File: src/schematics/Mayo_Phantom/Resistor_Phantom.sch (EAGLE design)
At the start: 178 parts, among them J1 22-27-2041-04, K1 AQY22SOP, K2 AQY22SOP, K3 AQY22SOP, X1 DSUBIN

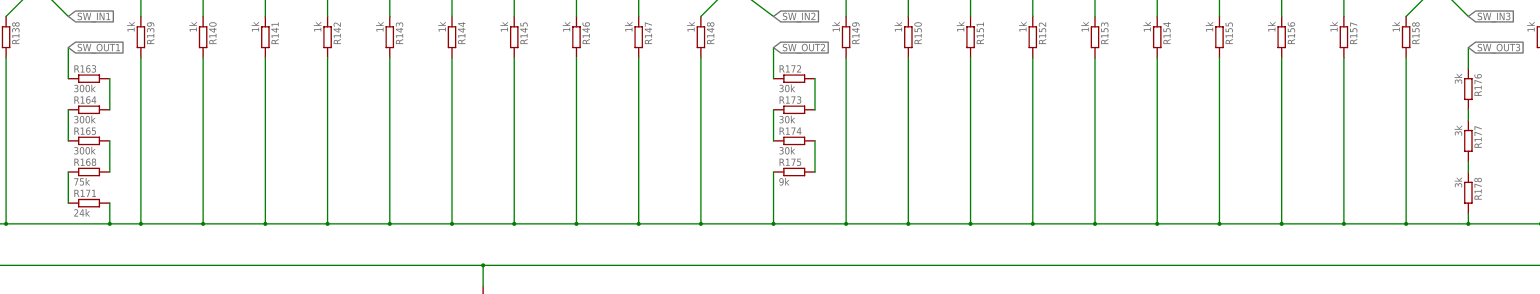
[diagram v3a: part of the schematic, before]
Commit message: changed resistor values in schematic
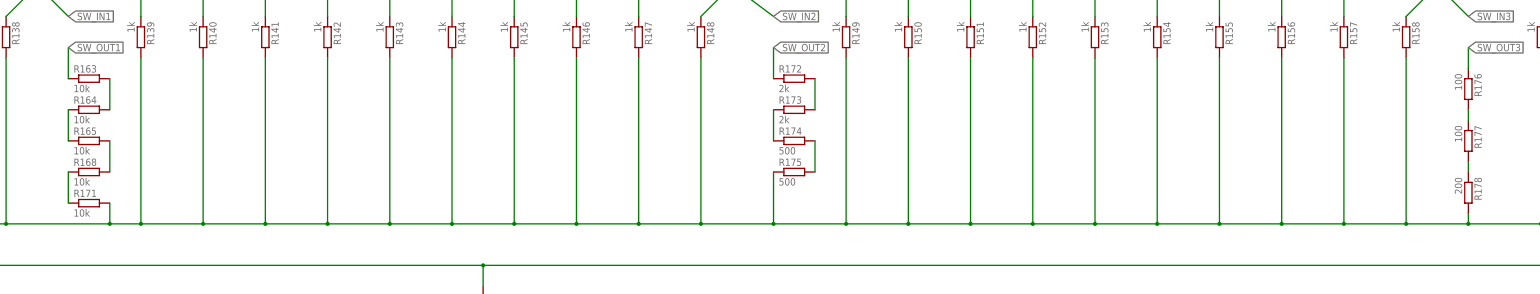
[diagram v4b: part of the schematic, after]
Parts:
- R163, R164, R165: value 300k -> 10k
- R168: value 75k -> 10k
- R171: value 24k -> 10k
- R172, R173: value 30k -> 2k
- R174: value 30k -> 500
- R175: value 9k -> 500
- R176, R177: value 3k -> 100
- R178: value 3k -> 200
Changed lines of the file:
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@@
 <grid distance="0.1" unitdist="inch" unit="inch" style="lines" multiple="1" display="no" altdistance="0.01" altunitdist="inch" altunit="inch"/>
 <layers>
-<layer number="1" name="Top" color="4" fill="1" visible="yes" active="no"/>
-<layer number="2" name="Route2" color="1" fill="3" visible="yes" active="no"/>
-<layer number="3" name="Route3" color="4" fill="3" visible="yes" active="no"/>
-<layer number="4" name="Route4" color="1" fill="4" visible="yes" active="no"/>
-<layer number="5" name="Route5" color="4" fill="4" visible="yes" active="no"/>
-<layer number="6" name="Route6" color="1" fill="8" visible="yes" active="no"/>
-<layer number="7" name="Route7" color="4" fill="8" visible="yes" active="no"/>
-<layer number="8" name="Route8" color="1" fill="2" visible="yes" active="no"/>
-<layer number="9" name="Route9" color="4" fill="2" visible="yes" active="no"/>
-<layer number="10" name="Route10" color="1" fill="7" visible="yes" active="no"/>
-<layer number="11" name="Route11" color="4" fill="7" visible="yes" active="no"/>
-<layer number="12" name="Route12" color="1" fill="5" visible="yes" active="no"/>
-<layer number="13" name="Route13" color="4" fill="5" visible="yes" active="no"/>
-<layer number="14" name="Route14" color="1" fill="6" visible="yes" active="no"/>
-<layer number="15" name="Route15" color="4" fill="6" visible="yes" active="no"/>
-<layer number="16" name="Bottom" color="1" fill="1" visible="yes" active="no"/>
-<layer number="17" name="Pads" color="2" fill="1" visible="yes" active="no"/>
-<layer number="18" name="Vias" color="2" fill="1" visible="yes" active="no"/>
-<layer number="19" name="Unrouted" color="6" fill="1" visible="yes" active="no"/>
-<layer number="20" name="Dimension" color="15" fill="1" visible="yes" active="no"/>
-<layer number="21" name="tPlace" color="7" fill="1" visible="yes" active="no"/>
-<layer number="22" name="bPlace" color="7" fill="1" visible="yes" active="no"/>
-<layer number="23" name="tOrigins" color="15" fill="1" visible="yes" active="no"/>
-<layer number="24" name="bOrigins" color="15" fill="1" visible="yes" active="no"/>
-<layer number="25" name="tNames" color="7" fill="1" visible="yes" active="no"/>
-<layer number="26" name="bNames" color="7" fill="1" visible="yes" active="no"/>
-<layer number="27" name="tValues" color="7" fill="1" visible="yes" active="no"/>
-<layer number="28" name="bValues" color="7" fill="1" visible="yes" active="no"/>
+<layer number="1" name="Top" color="4" fill="1" visible="no" active="no"/>
+<layer number="2" name="Route2" color="1" fill="3" visible="no" active="no"/>
+<layer number="3" name="Route3" color="4" fill="3" visible="no" active="no"/>
+<layer number="4" name="Route4" color="1" fill="4" visible="no" active="no"/>
+<layer number="5" name="Route5" color="4" fill="4" visible="no" active="no"/>
+<layer number="6" name="Route6" color="1" fill="8" visible="no" active="no"/>
+<layer number="7" name="Route7" color="4" fill="8" visible="no" active="no"/>
+<layer number="8" name="Route8" color="1" fill="2" visible="no" active="no"/>
+<layer number="9" name="Route9" color="4" fill="2" visible="no" active="no"/>
+<layer number="10" name="Route10" color="1" fill="7" visible="no" active="no"/>
+<layer number="11" name="Route11" color="4" fill="7" visible="no" active="no"/>
+<layer number="12" name="Route12" color="1" fill="5" visible="no" active="no"/>
+<layer number="13" name="Route13" color="4" fill="5" visible="no" active="no"/>
+<layer number="14" name="Route14" color="1" fill="6" visible="no" active="no"/>
+<layer number="15" name="Route15" color="4" fill="6" visible="no" active="no"/>
+<layer number="16" name="Bottom" color="1" fill="1" visible="no" active="no"/>
+<layer number="17" name="Pads" color="2" fill="1" visible="no" active="no"/>
+<layer number="18" name="Vias" color="2" fill="1" visible="no" active="no"/>
+<layer number="19" name="Unrouted" color="6" fill="1" visible="no" active="no"/>
+<layer number="20" name="Dimension" color="15" fill="1" visible="no" active="no"/>
+<layer number="21" name="tPlace" color="7" fill="1" visible="no" active="no"/>
+<layer number="22" name="bPlace" color="7" fill="1" visible="no" active="no"/>
+<layer number="23" name="tOrigins" color="15" fill="1" visible="no" active="no"/>
+<layer number="24" name="bOrigins" color="15" fill="1" visible="no" active="no"/>
+<layer number="25" name="tNames" color="7" fill="1" visible="no" active="no"/>
+<layer number="26" name="bNames" color="7" fill="1" visible="no" active="no"/>
+<layer number="27" name="tValues" color="7" fill="1" visible="no" active="no"/>
+<layer number="28" name="bValues" color="7" fill="1" visible="no" active="no"/>
 <layer number="29" name="tStop" color="7" fill="3" visible="no" active="no"/>
 <layer number="30" name="bStop" color="7" fill="6" visible="no" active="no"/>
@@
 <layer number="35" name="tGlue" color="7" fill="4" visible="no" active="no"/>
 <layer number="36" name="bGlue" color="7" fill="5" visible="no" active="no"/>
-<layer number="37" name="tTest" color="7" fill="1" visible="yes" active="no"/>
-<layer number="38" name="bTest" color="7" fill="1" visible="yes" active="no"/>
+<layer number="37" name="tTest" color="7" fill="1" visible="no" active="no"/>
+<layer number="38" name="bTest" color="7" fill="1" visible="no" active="no"/>
 <layer number="39" name="tKeepout" color="4" fill="11" visible="no" active="no"/>
 <layer number="40" name="bKeepout" color="1" fill="11" visible="no" active="no"/>
@@
 <layer number="44" name="Drills" color="7" fill="1" visible="no" active="no"/>
 <layer number="45" name="Holes" color="7" fill="1" visible="no" active="no"/>
-<layer number="46" name="Milling" color="3" fill="1" visible="yes" active="no"/>
-<layer number="47" name="Measures" color="7" fill="1" visible="yes" active="no"/>
-<layer number="48" name="Document" color="7" fill="1" visible="yes" active="no"/>
-<layer number="49" name="Reference" color="7" fill="1" visible="yes" active="no"/>
-<layer number="51" name="tDocu" color="7" fill="1" visible="yes" active="no"/>
-<layer number="52" name="bDocu" color="7" fill="1" visible="yes" active="no"/>
+<layer number="46" name="Milling" color="3" fill="1" visible="no" active="no"/>
+<layer number="47" name="Measures" color="7" fill="1" visible="no" active="no"/>
+<layer number="48" name="Document" color="7" fill="1" visible="no" active="no"/>
+<layer number="49" name="Reference" color="7" fill="1" visible="no" active="no"/>
+<layer number="51" name="tDocu" color="7" fill="1" visible="no" active="no"/>
+<layer number="52" name="bDocu" color="7" fill="1" visible="no" active="no"/>
 <layer number="90" name="Modules" color="5" fill="1" visible="yes" active="yes"/>
 <layer number="91" name="Nets" color="2" fill="1" visible="yes" active="yes"/>
@@
 <part name="K2" library="relay" deviceset="AQY*" device="SOP" technology="22" value="AQY22SOP"/>
 <part name="K3" library="relay" deviceset="AQY*" device="SOP" technology="22" value="AQY22SOP"/>
-<part name="R163" library="rcl" deviceset="R-EU_" device="R0402" value="300k"/>
-<part name="R164" library="rcl" deviceset="R-EU_" device="R0402" value="300k"/>
-<part name="R165" library="rcl" deviceset="R-EU_" device="R0402" value="300k"/>
-<part name="R168" library="rcl" deviceset="R-EU_" device="R0402" value="75k"/>
-<part name="R171" library="rcl" deviceset="R-EU_" device="R0402" value="24k"/>
-<part name="R172" library="rcl" deviceset="R-EU_" device="R0402" value="30k"/>
-<part name="R173" library="rcl" deviceset="R-EU_" device="R0402" value="30k"/>
-<part name="R174" library="rcl" deviceset="R-EU_" device="R0402" value="30k"/>
-<part name="R175" library="rcl" deviceset="R-EU_" device="R0402" value="9k"/>
-<part name="R176" library="rcl" deviceset="R-EU_" device="R0402" value="3k"/>
-<part name="R177" library="rcl" deviceset="R-EU_" device="R0402" value="3k"/>
-<part name="R178" library="rcl" deviceset="R-EU_" device="R0402" value="3k"/>
+<part name="R163" library="rcl" deviceset="R-EU_" device="R0402" value="10k"/>
+<part name="R164" library="rcl" deviceset="R-EU_" device="R0402" value="10k"/>
+<part name="R165" library="rcl" deviceset="R-EU_" device="R0402" value="10k"/>
+<part name="R168" library="rcl" deviceset="R-EU_" device="R0402" value="10k"/>
+<part name="R171" library="rcl" deviceset="R-EU_" device="R0402" value="10k"/>
+<part name="R172" library="rcl" deviceset="R-EU_" device="R0402" value="2k"/>
+<part name="R173" library="rcl" deviceset="R-EU_" device="R0402" value="2k"/>
+<part name="R174" library="rcl" deviceset="R-EU_" device="R0402" value="500"/>
+<part name="R175" library="rcl" deviceset="R-EU_" device="R0402" value="500"/>
+<part name="R176" library="rcl" deviceset="R-EU_" device="R0402" value="100"/>
+<part name="R177" library="rcl" deviceset="R-EU_" device="R0402" value="100"/>
+<part name="R178" library="rcl" deviceset="R-EU_" device="R0402" value="200"/>
 <part name="J1" library="con-molex" deviceset="22-?-04" device="27-2041"/>
 </parts>
